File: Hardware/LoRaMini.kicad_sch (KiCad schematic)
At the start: 59 parts, among them J2 Conn_01x01_Female, J3 USB4125-GF-A_REVA2, Q1 Q_PMOS_GSD, Q2 Q_NMOS_GSD, U1 BQ25060, U2 NCP170ASN330T2G_, U3 STM32G071KxU, U4 RFM95W-868S2, Y1 32KHz

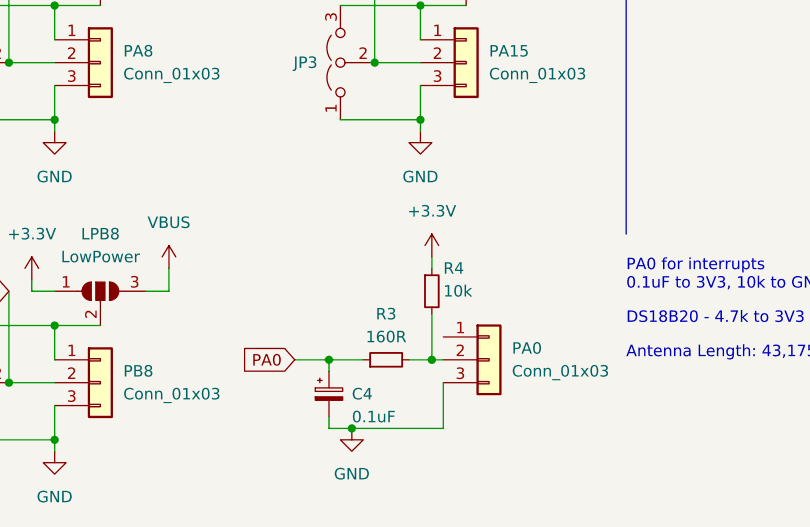
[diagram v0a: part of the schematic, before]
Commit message: fixed PA0
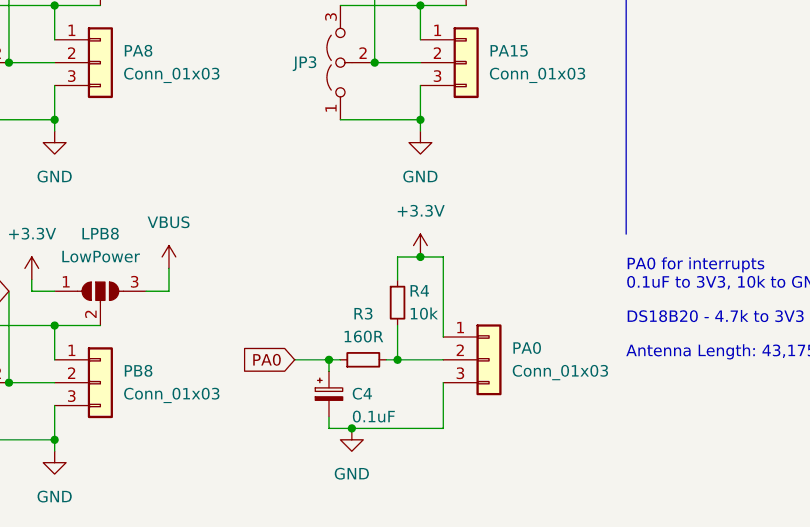
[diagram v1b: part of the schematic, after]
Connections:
- net +3V3: now also PA0.1 (Pin_1)
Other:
- moved on the sheet: R3, R4
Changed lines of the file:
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@@
   (junction (at 229.87 153.67) (diameter 0) (color 0 0 0 0)
   )
-  (junction (at 157.48 179.07) (diameter 0) (color 0 0 0 0)
-  )
   (junction (at 156.21 139.7) (diameter 0) (color 0 0 0 0)
   )
@@
   (junction (at 157.48 106.68) (diameter 0) (color 0 0 0 0)
   )
+  (junction (at 156.21 167.64) (diameter 0) (color 0 0 0 0)
+  )
   (junction (at 33.02 54.61) (diameter 0) (color 0 0 0 0)
   )
@@
   )
   (junction (at 220.98 20.32) (diameter 0) (color 0 0 0 0)
+  )
+  (junction (at 153.67 179.07) (diameter 0) (color 0 0 0 0)
   )
   (junction (at 110.49 146.05) (diameter 0) (color 0 0 0 0)
@@
     (stroke (width 0) (type default) (color 0 0 0 0))
   )
-  (wire (pts (xy 157.48 179.07) (xy 158.75 179.07))
-    (stroke (width 0) (type default) (color 0 0 0 0))
-  )
   (wire (pts (xy 57.15 36.83) (xy 57.15 39.37))
     (stroke (width 0) (type default) (color 0 0 0 0))
@@
     (stroke (width 0) (type default) (color 0 0 0 0))
   )
+  (wire (pts (xy 153.67 179.07) (xy 158.75 179.07))
+    (stroke (width 0) (type default) (color 0 0 0 0))
+  )
   (wire (pts (xy 142.24 179.07) (xy 146.05 179.07))
     (stroke (width 0) (type default) (color 0 0 0 0))
@@
     (stroke (width 0) (type default) (color 0 0 0 0))
   )
-  (wire (pts (xy 154.94 179.07) (xy 157.48 179.07))
+  (wire (pts (xy 152.4 179.07) (xy 153.67 179.07))
     (stroke (width 0) (type default) (color 0 0 0 0))
   )
@@
     (stroke (width 0) (type default) (color 0 0 0 0))
   )
+  (wire (pts (xy 158.75 167.64) (xy 156.21 167.64))
+    (stroke (width 0) (type default) (color 0 0 0 0))
+  )
   (wire (pts (xy 214.63 130.81) (xy 217.17 130.81))
     (stroke (width 0) (type default) (color 0 0 0 0))
@@
     (stroke (width 0) (type default) (color 0 0 0 0))
   )
-  (wire (pts (xy 157.48 173.99) (xy 157.48 179.07))
-    (stroke (width 0) (type default) (color 0 0 0 0))
-  )
   (wire (pts (xy 265.43 62.23) (xy 273.05 62.23))
     (stroke (width 0) (type default) (color 0 0 0 0))
@@
     (stroke (width 0) (type default) (color 0 0 0 0))
   )
-  (wire (pts (xy 146.05 179.07) (xy 149.86 179.07))
+  (wire (pts (xy 146.05 179.07) (xy 147.32 179.07))
     (stroke (width 0) (type default) (color 0 0 0 0))
   )
@@
     (stroke (width 0) (type default) (color 0 0 0 0))
   )
+  (wire (pts (xy 153.67 170.18) (xy 153.67 167.64))
+    (stroke (width 0) (type default) (color 0 0 0 0))
+  )
   (wire (pts (xy 148.59 44.45) (xy 148.59 43.18))
     (stroke (width 0) (type default) (color 0 0 0 0))
@@
     (stroke (width 0) (type default) (color 0 0 0 0))
   )
-  (wire (pts (xy 157.48 167.64) (xy 157.48 168.91))
+  (wire (pts (xy 153.67 167.64) (xy 156.21 167.64))
+    (stroke (width 0) (type default) (color 0 0 0 0))
+  )
+  (wire (pts (xy 158.75 176.53) (xy 158.75 167.64))
     (stroke (width 0) (type default) (color 0 0 0 0))
   )
@@
   )
   (wire (pts (xy 71.12 171.45) (xy 71.12 181.61))
+    (stroke (width 0) (type default) (color 0 0 0 0))
+  )
+  (wire (pts (xy 153.67 175.26) (xy 153.67 179.07))
     (stroke (width 0) (type default) (color 0 0 0 0))
   )
@@
     (pin "1")
   )
-  (symbol (lib_id "power:+3.3V") (at 157.48 167.64 0) (unit 1)
-    (in_bom yes) (on_board yes) (fields_autoplaced)
-    (property "Reference" "#PWR0123" (id 0) (at 157.48 171.45 0)
-      (effects (font (size 1.27 1.27)) hide)
-    )
-    (property "Value" "+3.3V" (id 1) (at 157.48 162.56 0))
-    (property "Footprint" "" (id 2) (at 157.48 167.64 0)
-      (effects (font (size 1.27 1.27)) hide)
-    )
-    (property "Datasheet" "" (id 3) (at 157.48 167.64 0)
+  (symbol (lib_id "power:+3.3V") (at 156.21 167.64 0) (unit 1)
+    (in_bom yes) (on_board yes) (fields_autoplaced)
+    (property "Reference" "#PWR0123" (id 0) (at 156.21 171.45 0)
+      (effects (font (size 1.27 1.27)) hide)
+    )
+    (property "Value" "+3.3V" (id 1) (at 156.21 162.56 0))
+    (property "Footprint" "" (id 2) (at 156.21 167.64 0)
+      (effects (font (size 1.27 1.27)) hide)
+    )
+    (property "Datasheet" "" (id 3) (at 156.21 167.64 0)
       (effects (font (size 1.27 1.27)) hide)
     )
@@
     (pin "1")
   )
-  (symbol (lib_id "Device:R_Small") (at 152.4 179.07 90) (unit 1)
+  (symbol (lib_id "Device:R_Small") (at 149.86 179.07 90) (unit 1)
     (in_bom yes) (on_board yes)
-    (property "Reference" "R3" (id 0) (at 152.4 173.99 90))
-    (property "Value" "160R" (id 1) (at 152.4 176.53 90))
-    (property "Footprint" "Resistor_SMD:R_0805_2012Metric" (id 2) (at 152.4 179.07 0)
-      (effects (font (size 1.27 1.27)) hide)
-    )
-    (property "Datasheet" "~" (id 3) (at 152.4 179.07 0)
+    (property "Reference" "R3" (id 0) (at 149.86 173.99 90))
+    (property "Value" "160R" (id 1) (at 149.86 176.53 90))
+    (property "Footprint" "Resistor_SMD:R_0805_2012Metric" (id 2) (at 149.86 179.07 0)
+      (effects (font (size 1.27 1.27)) hide)
+    )
+    (property "Datasheet" "~" (id 3) (at 149.86 179.07 0)
       (effects (font (size 1.27 1.27)) hide)
     )
@@
     (pin "3")
   )
-  (symbol (lib_id "Device:R_Small") (at 157.48 171.45 0) (unit 1)
+  (symbol (lib_id "Device:R_Small") (at 153.67 172.72 0) (unit 1)
     (in_bom yes) (on_board yes)
-    (property "Reference" "R4" (id 0) (at 158.75 168.91 0)
-      (effects (font (size 1.27 1.27)) (justify left))
-    )
-    (property "Value" "10k" (id 1) (at 158.75 171.45 0)
-      (effects (font (size 1.27 1.27)) (justify left))
-    )
-    (property "Footprint" "Resistor_SMD:R_0805_2012Metric" (id 2) (at 157.48 171.45 0)
-      (effects (font (size 1.27 1.27)) hide)
-    )
-    (property "Datasheet" "~" (id 3) (at 157.48 171.45 0)
-      (effects (font (size 1.27 1.27)) hide)
-    )
+    (property "Reference" "R4" (id 0) (at 154.94 171.45 0)
+      (effects (font (size 1.27 1.27)) (justify left))
+    )
+    (property "Value" "10k" (id 1) (at 154.94 173.99 0)
+      (effects (font (size 1.27 1.27)) (justify left))
+    )
+    (property "Footprint" "Resistor_SMD:R_0805_2012Metric" (id 2) (at 153.67 172.72 0)
+      (effects (font (size 1.27 1.27)) hide)
+    )
+    (property "Datasheet" "~" (id 3) (at 153.67 172.72 0)
+      (effects (font (size 1.27 1.27)) hide)
+    )
